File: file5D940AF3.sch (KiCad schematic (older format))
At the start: 129 parts, among them CN1 KEYBOARD_20PIN_MALE, CN10 LED_CONNECTOR, CN2 USER_PORT_CON, CN3 CASSETTE_PORT_CON, CN4 SERIAL_BUS_CON, CN7 POWER_CON, CN8 CONTROL_PORT, CN9 CONTROL_PORT, Q1 2SC1815, Q2 2SC1815, Q3 TP298/2SD880, Q7 2SC1815, SW1 POWER_SWITCH, U1 CIA_U1, U2 CIA_U2, U20 556, U27 7408_U27, U28 4066_U28, U29 74LS74, U30 74LS193, U31 74LS629N, U32 MC4044, U7 6510_MPU, U8 7406N, Y1 Crystal

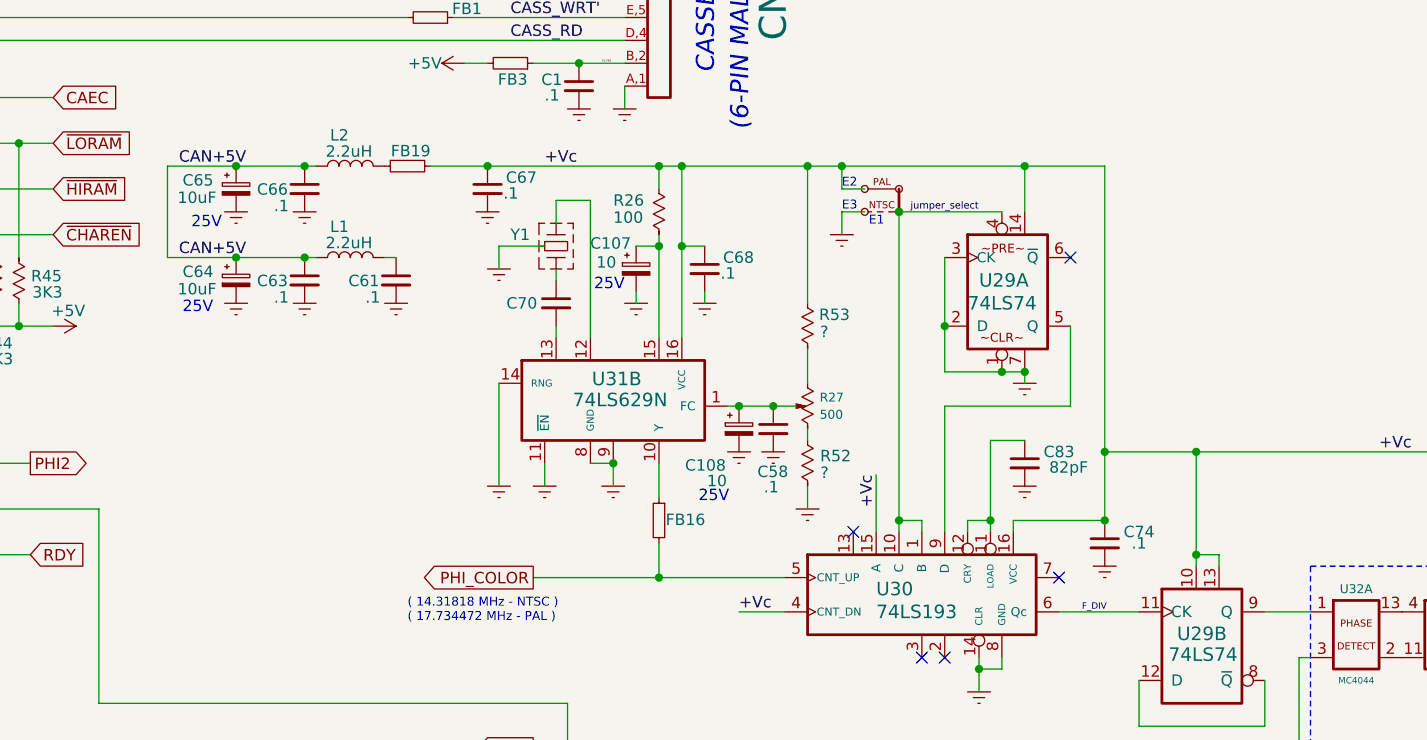
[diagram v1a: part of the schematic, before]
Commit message: AV connector, Not used parts, pdf update
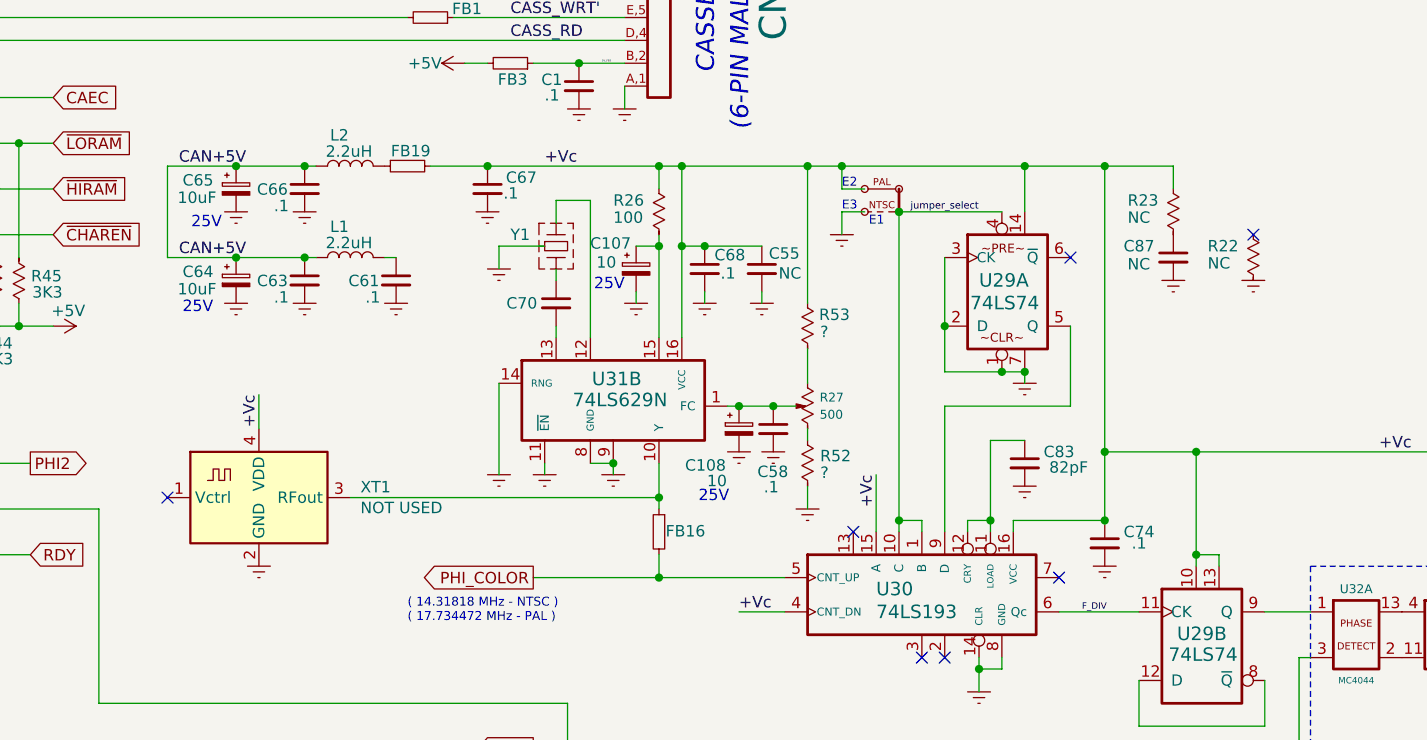
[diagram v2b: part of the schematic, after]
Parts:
- added C55, C87: NC, KU-14194HB-RevB-KiCad:CAP_P5.08mm, symbol Device:C_Small
- added R22, R23: NC, KU-14194HB-RevB-KiCad:RESISTOR, symbol KU-schematics-library:R_US_CUSTOM
- added XT1: NOT USED, KU-14194HB-RevB-KiCad:DIP4_DIP14_but_4_pins, symbol Oscillator:ABLNO
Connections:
- net +Vc: now also C55.1, R23.1, XT1.4 (VDD)
- net Earth: now also C55.2, C87.2, R22.2, XT1.2 (GND)
- net at FB16.1, U31.10 (Y): now also XT1.3 (RFout)
- new net: C87.1, R23.2
- no-connect marks 8 -> 10
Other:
- moved on the sheet: FB16
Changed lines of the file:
@@
 Sheet 2 3
 Title "C64 Motherboard KU-14194HB"
-Date "2019-09-28"
+Date "2019-09-29"
 Rev ""
 Comp "Commodore 1982"
@@
 AR Path="/5E4FA2E4" Ref="C?"  Part="1"
 AR Path="/5D940AF4/5E4FA2E4" Ref="C68"  Part="1"
-F 0 "C68" H 11048 3450 50  0000 C CNN
+F 0 "C68" H 11010 3461 50  0000 C CNN
 F 1 ".1" H 11002 3381 50  0000 C CNN
 F 2 "KU-14194HB-RevB-KiCad:CAP_P5.08mm" H 10900 3400 50  0001 C CNN
@@
 $EndComp
 Wire Wire Line
-	10700 4400 10700 4250
+	10700 4450 10700 4400
 $Comp
 L KU-schematics-library:FERRITE_NARROW FB16
 U 1 1 5E2F7729
-P 10700 4500
-F 0 "FB16" V 10697 4529 50  0000 L CNN
-F 1 "FERRITE_NARROW" H 10650 4400 50  0001 C CNN
-F 2 "KU-14194HB-RevB-KiCad:FERRITE_BEAD_TH_P12.7mm" H 10700 4500 50  0001 C CNN
-F 3 "" H 10700 4500 50  0001 C CNN
-	1    10700 4500
+P 10700 4550
+F 0 "FB16" V 10697 4579 50  0000 L CNN
+F 1 "FERRITE_NARROW" H 10650 4450 50  0001 C CNN
+F 2 "KU-14194HB-RevB-KiCad:FERRITE_BEAD_TH_P12.7mm" H 10700 4550 50  0001 C CNN
+F 3 "" H 10700 4550 50  0001 C CNN
+	1    10700 4550
 	0    1    1    0
 $EndComp
 Wire Wire Line
-	10000 3900 10000 4350
+	10000 3900 10000 4300
 $Comp
 L KU-14194HB-REV-B-KiCad-rescue:GND_SMALL-power U?
 U 1 1 5E2AF6CE
-P 10000 4350
+P 10000 4300
 AR Path="/5E2AF6CE" Ref="U?"  Part="1"
 AR Path="/5D940AF4/5E2AF6CE" Ref="#U0156"  Part="1"
-F 0 "#U0156" H 10000 4350 50  0001 C CNN
-F 1 "GND_SMALL" H 10000 4350 50  0001 C CNN
-F 2 "" H 10000 4350 50  0001 C CNN
-F 3 "" H 10000 4350 50  0001 C CNN
-	1    10000 4350
+F 0 "#U0156" H 10000 4300 50  0001 C CNN
+F 1 "GND_SMALL" H 10000 4300 50  0001 C CNN
+F 2 "" H 10000 4300 50  0001 C CNN
+F 3 "" H 10000 4300 50  0001 C CNN
+	1    10000 4300
 	1    0    0    -1
 $EndComp
 Wire Wire Line
-	10200 4350 10200 4250
+	10200 4300 10200 4250
 Connection ~ 10500 4250
 Wire Wire Line
 	10400 4250 10500 4250
 Wire Wire Line
-	10500 4250 10500 4350
+	10500 4250 10500 4300
 $Comp
 L KU-14194HB-REV-B-KiCad-rescue:GND_SMALL-power U?
 U 1 1 5E1D800F
-P 10500 4350
+P 10500 4300
 AR Path="/5E1D800F" Ref="U?"  Part="1"
 AR Path="/5D940AF4/5E1D800F" Ref="#U0157"  Part="1"
-F 0 "#U0157" H 10500 4350 50  0001 C CNN
-F 1 "GND_SMALL" H 10500 4350 50  0001 C CNN
-F 2 "" H 10500 4350 50  0001 C CNN
-F 3 "" H 10500 4350 50  0001 C CNN
-	1    10500 4350
+F 0 "#U0157" H 10500 4300 50  0001 C CNN
+F 1 "GND_SMALL" H 10500 4300 50  0001 C CNN
+F 2 "" H 10500 4300 50  0001 C CNN
+F 3 "" H 10500 4300 50  0001 C CNN
+	1    10500 4300
 	1    0    0    -1
 $EndComp
@@
 L KU-14194HB-REV-B-KiCad-rescue:GND_SMALL-power U?
 U 1 1 5E1D6D66
-P 10200 4350
+P 10200 4300
 AR Path="/5E1D6D66" Ref="U?"  Part="1"
 AR Path="/5D940AF4/5E1D6D66" Ref="#U0158"  Part="1"
-F 0 "#U0158" H 10200 4350 50  0001 C CNN
-F 1 "GND_SMALL" H 10200 4350 50  0001 C CNN
-F 2 "" H 10200 4350 50  0001 C CNN
-F 3 "" H 10200 4350 50  0001 C CNN
-	1    10200 4350
+F 0 "#U0158" H 10200 4300 50  0001 C CNN
+F 1 "GND_SMALL" H 10200 4300 50  0001 C CNN
+F 2 "" H 10200 4300 50  0001 C CNN
+F 3 "" H 10200 4300 50  0001 C CNN
+	1    10200 4300
 	1    0    0    -1
 $EndComp
@@
 Text GLabel 10150 4750 0    50   Output ~ 0
 PHI_COLOR
-Wire Wire Line
-	10150 4750 10700 4750
 $Comp
 L KU-schematics-library:R_POTMETER_US R27
@@
 Connection ~ 10800 2950
 Wire Wire Line
-	10700 4750 10700 4600
+	10700 4750 10700 4650
 Wire Wire Line
 	9700 6400 9700 6450
@@
 P 12250 3500
 F 0 "U29" H 12100 3550 59  0000 L CNN
-F 1 "74LS74" H 12050 3450 59  0000 L CNN
+F 1 "74LS74" H 12061 3451 59  0000 L CNN
 F 2 "KU-14194HB-RevB-KiCad:DIP14" H 12250 3500 39  0001 C CNN
 F 3 "" H 12250 3500 39  0001 C CNN
@@
 Text Label 8500 6400 0    50   ~ 0
 CAN+5V
+$Comp
+L Oscillator:ABLNO XT1
+U 1 1 5DA48A52
+P 8950 4400
+F 0 "XT1" H 9394 4446 50  0000 L CNN
+F 1 "NOT USED" H 9394 4355 50  0000 L CNN
+F 2 "KU-14194HB-RevB-KiCad:DIP4_DIP14_but_4_pins" H 8950 4050 50  0001 C CNN
+F 3 "https://abracon.com/Precisiontiming/ABLNO.pdf" H 8750 4500 50  0001 C CNN
+	1    8950 4400
+	1    0    0    -1
+$EndComp
+NoConn ~ 8550 4400
+$Comp
+L KU-14194HB-REV-B-KiCad-rescue:GND_SMALL-power U?
+U 1 1 5DB110FC
+P 8950 4700
+AR Path="/5DB110FC" Ref="U?"  Part="1"
+AR Path="/5D940AF4/5DB110FC" Ref="#U0236"  Part="1"
+F 0 "#U0236" H 8950 4700 50  0001 C CNN
+F 1 "GND_SMALL" H 8950 4700 50  0001 C CNN
+F 2 "" H 8950 4700 50  0001 C CNN
+F 3 "" H 8950 4700 50  0001 C CNN
+	1    8950 4700
+	1    0    0    -1
+$EndComp
+Wire Wire Line
+	8950 4100 8950 3950
+Text Label 8950 3950 3    50   ~ 0
++Vc
+Wire Wire Line
+	10700 4400 9350 4400
+Connection ~ 10700 4400
+Wire Wire Line
+	10700 4400 10700 4250
+Wire Wire Line
+	10150 4750 10700 4750
+$Comp
+L KU-schematics-library:R_US_CUSTOM R?
+U 1 1 5E0D17B1
+P 12950 3150
+AR Path="/5E0D17B1" Ref="R?"  Part="1"
+AR Path="/5D940AF4/5E0D17B1" Ref="R23"  Part="1"
+F 0 "R23" H 12750 3200 50  0000 L CNN
+F 1 "NC" H 12750 3125 50  0000 L CNN
+F 2 "KU-14194HB-RevB-KiCad:RESISTOR" H 12950 3150 50  0001 C CNN
+F 3 "" H 12950 3150 50  0001 C CNN
+	1    12950 3150
+	1    0    0    -1
+$EndComp
+Wire Wire Line
+	12950 3050 12950 2950
+Wire Wire Line
+	12950 2950 12650 2950
+Connection ~ 12650 2950
+$Comp
+L KU-14194HB-REV-B-KiCad-rescue:GND_SMALL-power #U?
+U 1 1 5E1390F2
+P 12950 3450
+AR Path="/5E1390F2" Ref="#U?"  Part="1"
+AR Path="/5D940AF4/5E1390F2" Ref="#U0238"  Part="1"
+F 0 "#U0238" H 12950 3450 50  0001 C CNN
+F 1 "GND_SMALL" H 12950 3450 50  0001 C CNN
+F 2 "" H 12950 3450 50  0001 C CNN
+F 3 "" H 12950 3450 50  0001 C CNN
+	1    12950 3450
+	1    0    0    -1
+$EndComp
+$Comp
+L KU-schematics-library:R_US_CUSTOM R?
+U 1 1 5E13986B
+P 13300 3350
+AR Path="/5E13986B" Ref="R?"  Part="1"
+AR Path="/5D940AF4/5E13986B" Ref="R22"  Part="1"
+F 0 "R22" H 13100 3400 50  0000 L CNN
+F 1 "NC" H 13100 3325 50  0000 L CNN
+F 2 "KU-14194HB-RevB-KiCad:RESISTOR" H 13300 3350 50  0001 C CNN
+F 3 "" H 13300 3350 50  0001 C CNN
+	1    13300 3350
+	1    0    0    -1
+$EndComp
+NoConn ~ 13300 3250
+$Comp
+L KU-14194HB-REV-B-KiCad-rescue:GND_SMALL-power #U?
+U 1 1 5E19F876
+P 13300 3450
+AR Path="/5E19F876" Ref="#U?"  Part="1"
+AR Path="/5D940AF4/5E19F876" Ref="#U0239"  Part="1"
+F 0 "#U0239" H 13300 3450 50  0001 C CNN
+F 1 "GND_SMALL" H 13300 3450 50  0001 C CNN
+F 2 "" H 13300 3450 50  0001 C CNN
+F 3 "" H 13300 3450 50  0001 C CNN
+	1    13300 3450
+	1    0    0    -1
+$EndComp
+$Comp
+L Device:C_Small C?
+U 1 1 5E2A761A
+P 11150 3400
+AR Path="/5E2A761A" Ref="C?"  Part="1"
+AR Path="/5D940AF4/5E2A761A" Ref="C55"  Part="1"
+F 0 "C55" H 11248 3468 50  0000 C CNN
+F 1 "NC" H 11273 3381 50  0000 C CNN
+F 2 "KU-14194HB-RevB-KiCad:CAP_P5.08mm" H 11150 3400 50  0001 C CNN
+F 3 "~" H 11150 3400 50  0001 C CNN
+	1    11150 3400
+	1    0    0    -1
+$EndComp
+Wire Wire Line
+	11150 3300 10900 3300
+Connection ~ 10900 3300
+$Comp
+L KU-14194HB-REV-B-KiCad-rescue:GND_SMALL-power #U?
+U 1 1 5E30D1DB
+P 11150 3550
+AR Path="/5E30D1DB" Ref="#U?"  Part="1"
+AR Path="/5D940AF4/5E30D1DB" Ref="#U0240"  Part="1"
+F 0 "#U0240" H 11150 3550 50  0001 C CNN
+F 1 "GND_SMALL" H 11150 3550 50  0001 C CNN
+F 2 "" H 11150 3550 50  0001 C CNN
+F 3 "" H 11150 3550 50  0001 C CNN
+	1    11150 3550
+	1    0    0    -1
+$EndComp
+Wire Wire Line
+	11150 3500 11150 3550
+$Comp
+L Device:C_Small C?
+U 1 1 5E0D1EF1
+P 12950 3350
+AR Path="/5E0D1EF1" Ref="C?"  Part="1"
+AR Path="/5D940AF4/5E0D1EF1" Ref="C87"  Part="1"
+F 0 "C87" H 12800 3400 50  0000 C CNN
+F 1 "NC" H 12799 3321 50  0000 C CNN
+F 2 "KU-14194HB-RevB-KiCad:CAP_P5.08mm" H 12950 3350 50  0001 C CNN
+F 3 "~" H 12950 3350 50  0001 C CNN
+	1    12950 3350
+	1    0    0    -1
+$EndComp
 Wire Bus Line
 	7750 7100 7750 7400

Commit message: Replica 1.0
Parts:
- Y1: footprint (none) -> KU-14194HB-RevB-KiCad:CRYSTAL
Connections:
- net BTNA\LP renamed BTNA\~LP~
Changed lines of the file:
@@
 Sheet 2 3
 Title "C64 Motherboard KU-14194HB"
-Date "2019-09-29"
-Rev ""
+Date "2019-10-05"
+Rev "1.0"
 Comp "Commodore 1982"
 Comment1 "Retraced and schematics by bwack 2019"
@@
 	1900 6900 2800 6900
 Text Label 1900 4700 0    50   Italic 0
-BTNA\LP
+BTNA\~LP~
 Text Label 1900 4600 0    50   Italic 0
 JOYA3
@@
 	3650 5100 5850 5100
 Text GLabel 4750 4700 2    50   Output ~ 0
-BTNA\LP
+BTNA\~LP~
 Wire Wire Line
 	5850 6800 2900 6800
@@
 F 0 "Y1" H 10050 3350 50  0000 L CNN
 F 1 "Crystal" H 10250 3150 50  0001 C CNN
-F 2 "" H 10250 3300 50  0001 C CNN
+F 2 "KU-14194HB-RevB-KiCad:CRYSTAL" H 10250 3300 50  0001 C CNN
 F 3 "" H 10250 3300 50  0001 C CNN
 	1    10250 3300
@@
 Connection ~ 9150 2950
 Wire Wire Line
-	8850 2950 9150 2950
+	8850 2950 9000 2950
 $Comp
 L Device:CP_Small C65
@@
 	1    0    0    -1
 $EndComp
+Text GLabel 9050 2700 2    39   Output ~ 0
+CAN+5V
+Wire Wire Line
+	9050 2700 9000 2700
+Wire Wire Line
+	9000 2700 9000 2950
+Connection ~ 9000 2950
+Wire Wire Line
+	9000 2950 9150 2950
 Wire Bus Line
 	7750 7100 7750 7400
